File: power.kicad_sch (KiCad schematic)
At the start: 11 parts, among them J2 USB_C_Receptacle_USB2.0_16P, J3 BATTERY, U5 LD1117S33TR_SOT223

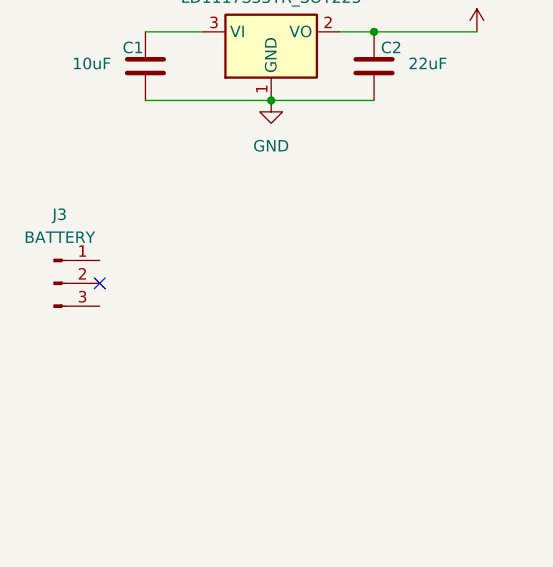
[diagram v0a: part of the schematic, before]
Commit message: battery polarity
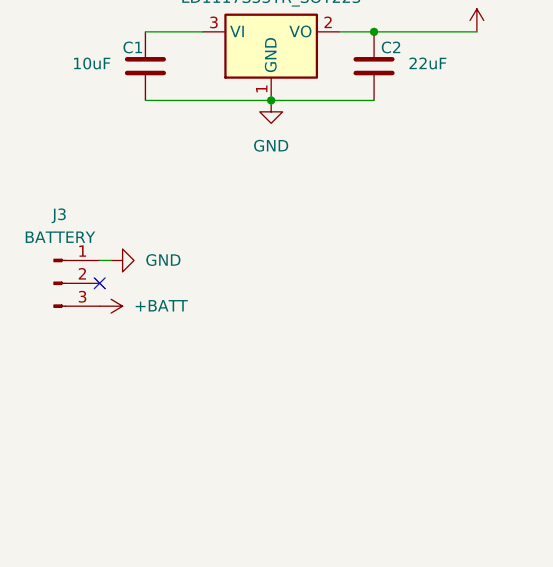
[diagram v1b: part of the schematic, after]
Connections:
- net GND: now also J3.1 (Pin_1)
- net +BATT: now reaches J3.3 (Pin_3)
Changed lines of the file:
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@@
+	(wire
+		(pts
+			(xy 49.53 69.85) (xy 50.8 69.85)
+		)
+		(stroke
+			(width 0)
+			(type default)
+		)
+	)
 	(wire
 		(pts
@@
 	)
 	(symbol
+		(lib_id "power:GND")
+		(at 50.8 69.85 90)
+		(unit 1)
+		(exclude_from_sim no)
+		(in_bom yes)
+		(on_board yes)
+		(dnp no)
+		(fields_autoplaced yes)
+		(property "Reference" "#PWR028"
+			(at 57.15 69.85 0)
+			(effects
+				(font
+					(size 1.27 1.27)
+				)
+				(hide yes)
+			)
+		)
+		(property "Value" "GND"
+			(at 54.61 69.8499 90)
+			(effects
+				(font
+					(size 1.27 1.27)
+				)
+				(justify right)
+			)
+		)
+		(property "Footprint" ""
+			(at 50.8 69.85 0)
+			(effects
+				(font
+					(size 1.27 1.27)
+				)
+				(hide yes)
+			)
+		)
+		(property "Datasheet" ""
+			(at 50.8 69.85 0)
+			(effects
+				(font
+					(size 1.27 1.27)
+				)
+				(hide yes)
+			)
+		)
+		(property "Description" "Power symbol creates a global label with name \"GND\" , ground"
+			(at 50.8 69.85 0)
+			(effects
+				(font
+					(size 1.27 1.27)
+				)
+				(hide yes)
+			)
+		)
+		(pin "1"
+		)
+		(instances
+			(project ""
+				(path "/e9d3405d-3536-4ebc-8db6-e75908125fac/41ee46a8-d813-490e-b535-9d8ea207b7f8"
+					(reference "#PWR028")
+					(unit 1)
+				)
+			)
+		)
+	)
+	(symbol
 		(lib_id "Connector:USB_C_Receptacle_USB2.0_16P")
 		(at 167.64 55.88 0)
@@
 					(unit 1)
 				)
+			)
+		)
+	)
+	(symbol
+		(lib_id "power:+BATT")
+		(at 49.53 74.93 270)
+		(unit 1)
+		(exclude_from_sim no)
+		(in_bom yes)
+		(on_board yes)
+		(dnp no)
+		(fields_autoplaced yes)
+		(property "Reference" "#PWR027"
+			(at 45.72 74.93 0)
+			(effects
+				(font
+					(size 1.27 1.27)
+				)
+				(hide yes)
+			)
+		)
+		(property "Value" "+BATT"
+			(at 53.34 74.9299 90)
+			(effects
+				(font
+					(size 1.27 1.27)
+				)
+				(justify left)
+			)
+		)
+		(property "Footprint" ""
+			(at 49.53 74.93 0)
+			(effects
+				(font
+					(size 1.27 1.27)
+				)
+				(hide yes)
+			)
+		)
+		(property "Datasheet" ""
+			(at 49.53 74.93 0)
+			(effects
+				(font
+					(size 1.27 1.27)
+				)
+				(hide yes)
+			)
+		)
+		(property "Description" "Power symbol creates a global label with name \"+BATT\""
+			(at 49.53 74.93 0)
+			(effects
+				(font
+					(size 1.27 1.27)
+				)
+				(hide yes)
+			)
+		)
+		(pin "1"
+		)
+		(instances
+			(project ""
+				(path "/e9d3405d-3536-4ebc-8db6-e75908125fac/41ee46a8-d813-490e-b535-9d8ea207b7f8"
+					(reference "#PWR027")
+					(unit 1)
+				)

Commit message: power
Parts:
- added D4: BAV70, Package_TO_SOT_SMD:SOT-23, symbol Diode:BAV70
- added Q3: IRLML6402, Package_TO_SOT_SMD:SOT-23, symbol Transistor_FET:IRLML6402
- added R15: 100k, symbol Device:R
- added R16: 1k, symbol Device:R
- added R17: 10k, symbol Device:R
- added SW20: POWER_BUTTON, symbol Switch:SW_Push
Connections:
- net +3.3V: now also R17.1
- net +BATT: now also Q3.2 (S), R15.2
- net GND: now also SW20.1
- net at C1.1, U5.3 (VI): now also Q3.3 (D)
- new net: D4.2 (A), Q3.1 (G), R15.1, R16.2
- new net: D4.3 (K), SW20.2
- new net PWRBTN_DETECT: D4.1 (A), R17.2
- new net PWR_HOLD: R16.1
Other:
- moved on the sheet: C1, C2, J3, U5

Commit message: spi joke
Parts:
- added C8, C9: 1uF, symbol Device:C
- added R23: 1k, symbol Device:R
- added R24: 10k, symbol Device:R
- added TH1: NTC, symbol Device:Thermistor_NTC
- added U4: BQ21040DBV, Package_TO_SOT_SMD:SOT-23-6, symbol Battery_Management:BQ21040DBV
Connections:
- net +3.3V: now also R24.2
- net +BATT: now also C9.1, U4.2 (OUT)
- net GND: now also C8.2, C9.2, R23.2, TH1.2, U4.5 (GND)
- net USB_VBUS: now also C8.1, U4.6 (VIN)
- new net: R23.1, U4.4 (ISET)
- new net: TH1.1, U4.1 (TS)
- new net CHG_PIN: R24.1, U4.3 (~{CHG})

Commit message: buck converter
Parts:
- removed U5: LD1117S33TR_SOT223, Package_TO_SOT_SMD:SOT-223-3_TabPin2, symbol Regulator_Linear:LD1117S33TR_SOT223
- added C13: 22uF 16V X5R, Capacitor_SMD:C_1206_3216Metric, symbol Device:C
- added L1: 2.2uH, Inductor_SMD:L_6.3x6.3_H3, symbol Device:L_Iron
- added R26: 249k, symbol Device:R
- added R27: 54.9k, symbol Device:R
- added TP7: BATTERY, symbol Connector:TestPoint
- added U7: RT8059, Package_TO_SOT_SMD:TSOT-23-5_HandSoldering, symbol RT8059:RT8059
- C1: value 10uF -> 4.7uF; footprint (none) -> Capacitor_SMD:C_0603_1608Metric
- C2: value 22uF -> 0-8.2pF; footprint (none) -> Capacitor_SMD:C_0603_1608Metric_Pad1.08x0.95mm_HandSolder
- R4: footprint (none) -> Capacitor_SMD:C_0603_1608Metric_Pad1.08x0.95mm_HandSolder
- TH1: footprint (none) -> Connector_JST:JST_EH_B2B-EH-A_1x02_P2.50mm_Vertical
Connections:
- net +3.3V: now also C13.1, L1.2, R26.1
- net +BATT: now also TP7.1
- net GND: now also C13.2, R27.2, U7.2 (GND); no longer C2.2
- net at C1.1, Q3.3 (D): now also U7.1 (EN), U7.4 (VIN)
- new net: C2.2, R26.2, R27.1, U7.5 (FB)
- new net: L1.1, U7.3 (LX)
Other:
- moved on the sheet: D1, F1, J2, R4, R5, R6, R7

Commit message: eee:
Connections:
- net +VSW: now reaches C1.1, Q3.3 (D), U7.1 (EN), U7.4 (VIN)
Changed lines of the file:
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@@
+	(wire
+		(pts
+			(xy 152.4 72.39) (xy 152.4 74.93)
+		)
+		(stroke
+			(width 0)
+			(type default)
+		)
+	)
 	(wire
 		(pts
@@
 		(pts
 			(xy 58.42 153.67) (xy 58.42 154.94)
-		)
-		(stroke
-			(width 0)
-			(type default)
-		)
-	)
-	(wire
-		(pts
-			(xy 152.4 74.93) (xy 153.67 74.93)
 		)
 		(stroke
@@
 	(symbol
 		(lib_id "power:+3.3V")
-		(at 153.67 74.93 0)
+		(at 152.4 72.39 0)
 		(unit 1)
 		(exclude_from_sim no)
@@
 		(fields_autoplaced yes)
 		(property "Reference" "#PWR016"
-			(at 153.67 78.74 0)
+			(at 152.4 76.2 0)
 			(effects
 				(font
@@
 		)
 		(property "Value" "+3.3V"
-			(at 153.67 69.85 0)
+			(at 152.4 67.31 0)
 			(effects
 				(font
@@
 		)
 		(property "Footprint" ""
-			(at 153.67 74.93 0)
+			(at 152.4 72.39 0)
 			(effects
 				(font
@@
 		)
 		(property "Datasheet" ""
-			(at 153.67 74.93 0)
+			(at 152.4 72.39 0)
 			(effects
 				(font
@@
 		)
 		(property "Description" "Power symbol creates a global label with name \"+3.3V\""
-			(at 153.67 74.93 0)
+			(at 152.4 72.39 0)
 			(effects
 				(font
@@
 					(unit 1)
 				)
+			)
+		)
+	)
+	(symbol
+		(lib_id "power:+VSW")
+		(at 82.55 74.93 0)
+		(unit 1)
+		(exclude_from_sim no)
+		(in_bom yes)
+		(on_board yes)
+		(dnp no)
+		(fields_autoplaced yes)
+		(property "Reference" "#PWR042"
+			(at 82.55 78.74 0)
+			(effects
+				(font
+					(size 1.27 1.27)
+				)
+				(hide yes)
+			)
+		)
+		(property "Value" "+VSW"
+			(at 82.55 69.85 0)
+			(effects
+				(font
+					(size 1.27 1.27)
+				)
+			)
+		)
+		(property "Footprint" ""
+			(at 82.55 74.93 0)
+			(effects
+				(font
+					(size 1.27 1.27)
+				)
+				(hide yes)
+			)
+		)
+		(property "Datasheet" ""
+			(at 82.55 74.93 0)
+			(effects
+				(font
+					(size 1.27 1.27)
+				)
+				(hide yes)
+			)
+		)
+		(property "Description" "Power symbol creates a global label with name \"+VSW\""
+			(at 82.55 74.93 0)
+			(effects
+				(font
+					(size 1.27 1.27)
+				)
+				(hide yes)
+			)
+		)
+		(pin "1"
+		)
+		(instances
+			(project ""
+				(path "/e9d3405d-3536-4ebc-8db6-e75908125fac/41ee46a8-d813-490e-b535-9d8ea207b7f8"
+					(reference "#PWR042")
+					(unit 1)
+				)

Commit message: mblya
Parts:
- removed J2: USB_C_Receptacle_USB2.0_16P, symbol Connector:USB_C_Receptacle_USB2.0_16P
- removed Q3: IRLML6402, Package_TO_SOT_SMD:SOT-23, symbol Transistor_FET:IRLML6402
- added D4, D5: D_TVS, symbol Device:D_TVS
- added J5: USB_C_Receptacle_USB2.0_16P, symbol Connector:USB_C_Receptacle_USB2.0_16P
- renumbered C8 to C1, C9 to C2, C1 to C3, C2 to C4, C13 to C5, D4 to D1, D1 to D2, R24 to R10, R26 to R11, R27 to R12, R23 to R2, R17 to R3, R6 to R4, R15 to R5, R4 to R6, R5 to R7, R7 to R8, R16 to R9, U7 to U6
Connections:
- net +BATT: now also C3.1, U6.4 (VIN)
- net GND: now also R6.1, R7.1, D4.1 (A1), D5.1 (A1), J5.A1 (GND), J5.A12 (GND), J5.B1 (GND), J5.B12 (GND), J5.S1 (SHIELD); no longer R6.2, R7.2
- net USB_DN: now also D5.2 (A2), J5.A7 (D-), J5.B7 (D-)
- net USB_DP: now also D4.2 (A2), J5.A6 (D+), J5.B6 (D+)
- net at D2.2 (A2), F1.1: now also J5.A4 (VBUS), J5.A9 (VBUS), J5.B4 (VBUS), J5.B9 (VBUS)
- net at D1.2 (A), R5.1, R9.2: now also U6.1 (EN)
- net at R8.1: now also J5.A8 (SBU1)
- net at R4.1: now also J5.B8 (SBU2)
- removed net +VSW: C3.1, U6.1 (EN), U6.4 (VIN)
- new net: J5.A5 (CC1), R6.2
- new net: J5.B5 (CC2), R7.2
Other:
- moved on the sheet: D2, R4, R6, R7, R8

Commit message: SCHEMATIC
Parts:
- added BUCK_BAT, BUCK_POST, BUCK_VBUS, CHRG_VBUS: SolderJumper_2_Open, Jumper:SolderJumper-2_P1.3mm_Open_Pad1.0x1.5mm, symbol Jumper:SolderJumper_2_Open
- R2: value 1k -> 680
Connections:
- net +3.3V: now also BUCK_POST.1 (A); no longer C4.1, L1.2, R11.1
- net +BATT: now also BUCK_BAT.2 (B); no longer C3.1, U6.4 (VIN)
- net USB_VBUS: now also BUCK_VBUS.1 (A), CHRG_VBUS.1 (A); no longer C1.1, U4.6 (VIN)
- new net: BUCK_POST.2 (B), C4.1, L1.2, R11.1
- new net: BUCK_BAT.1 (A), BUCK_VBUS.2 (B), C3.1, U6.4 (VIN)
- new net: C1.1, CHRG_VBUS.2 (B), U4.6 (VIN)
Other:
- note added: "USB"

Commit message: PCB BEGINNNING
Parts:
- C1, C2: footprint (none) -> Capacitor_SMD:C_0603_1608Metric_Pad1.08x0.95mm_HandSolder
- C3: footprint Capacitor_SMD:C_0603_1608Metric -> Capacitor_SMD:C_0603_1608Metric_Pad1.08x0.95mm_HandSolder
- D2, D4, D5: footprint (none) -> Diode_SMD:D_0603_1608Metric_Pad1.05x0.95mm_HandSolder
- F1: footprint (none) -> Fuse:Fuse_1210_3225Metric
- J5: footprint (none) -> UJ20-C-G-MSMT-TR-68:CUI_UJ20-C-G-MSMT-TR-68
- R10, R11, R12, R2, R3, R4, R5, R7, R8, R9: footprint (none) -> Resistor_SMD:R_0603_1608Metric_Pad0.98x0.95mm_HandSolder
- R6: footprint Capacitor_SMD:C_0603_1608Metric_Pad1.08x0.95mm_HandSolder -> Resistor_SMD:R_0603_1608Metric_Pad0.98x0.95mm_HandSolder
- SW20: footprint (none) -> PTS526_SM08_SMTR2_LFS:SW_PTS526_SM08_SMTR2_LFS
- TP7: footprint (none) -> TestPoint:TestPoint_Pad_D1.0mm
- renumbered BUCK_BAT to BUCK_BAT1, BUCK_POST to BUCK_POST1, BUCK_VBUS to BUCK_VBUS1, CHRG_VBUS to CHRG_VBUS1
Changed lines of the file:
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@@
 			)
 		)
-		(property "Footprint" ""
+		(property "Footprint" "Diode_SMD:D_0603_1608Metric_Pad1.05x0.95mm_HandSolder"
 			(at 76.2 173.99 0)
 			(effects
@@
 			)
 		)
-		(property "Footprint" ""
+		(property "Footprint" "Resistor_SMD:R_0603_1608Metric_Pad0.98x0.95mm_HandSolder"
 			(at 32.512 104.14 90)
 			(effects
@@
 			)
 		)
-		(property "Footprint" ""
+		(property "Footprint" "Diode_SMD:D_0603_1608Metric_Pad1.05x0.95mm_HandSolder"
 			(at 71.12 173.99 0)
 			(effects
@@
 			)
 		)
-		(property "Footprint" ""
+		(property "Footprint" "Diode_SMD:D_0603_1608Metric_Pad1.05x0.95mm_HandSolder"
 			(at 83.82 173.99 0)
 			(effects
@@
 			)
 		)
-		(property "Footprint" ""
+		(property "Footprint" "Resistor_SMD:R_0603_1608Metric_Pad0.98x0.95mm_HandSolder"
 			(at 140.462 95.25 90)
 			(effects
@@
 			)
 		)
-		(property "Footprint" "Capacitor_SMD:C_0603_1608Metric"
+		(property "Footprint" "Capacitor_SMD:C_0603_1608Metric_Pad1.08x0.95mm_HandSolder"
 			(at 87.3252 82.55 0)
 			(effects
@@
 			)
 		)
-		(property "Footprint" ""
+		(property "Footprint" "Resistor_SMD:R_0603_1608Metric_Pad0.98x0.95mm_HandSolder"
 			(at 60.452 71.12 90)
 			(effects
@@
 			)
 		)
-		(property "Footprint" ""
+		(property "Footprint" "Resistor_SMD:R_0603_1608Metric_Pad0.98x0.95mm_HandSolder"
 			(at 55.372 43.18 90)
 			(effects
@@
 			)
 		)
-		(property "Footprint" "Capacitor_SMD:C_0603_1608Metric_Pad1.08x0.95mm_HandSolder"
+		(property "Footprint" "Resistor_SMD:R_0603_1608Metric_Pad0.98x0.95mm_HandSolder"
 			(at 66.548 173.99 90)
 			(effects
@@
 			)
 		)
-		(property "Footprint" ""
+		(property "Footprint" "Fuse:Fuse_1210_3225Metric"
 			(at 93.98 138.43 0)
 			(effects
@@
 			)
 		)
-		(property "Footprint" ""
+		(property "Footprint" "PTS526_SM08_SMTR2_LFS:SW_PTS526_SM08_SMTR2_LFS"
 			(at 52.07 52.07 0)
 			(effects
@@
 			)
 		)
-		(property "Footprint" ""
+		(property "Footprint" "Capacitor_SMD:C_0603_1608Metric_Pad1.08x0.95mm_HandSolder"
 			(at 62.23 87.9348 0)
 			(effects
@@
 		(on_board yes)
 		(dnp no)
-		(property "Reference" "BUCK_VBUS"
+		(property "Reference" "BUCK_VBUS1"
 			(at 85.09 72.136 0)
 			(effects
@@
 			(project "okabephone"
 				(path "/e9d3405d-3536-4ebc-8db6-e75908125fac/4fc341b7-aab9-4bf1-942c-802f704f4f3e"
-					(reference "BUCK_VBUS")
+					(reference "BUCK_VBUS1")
 					(unit 1)
 				)
@@
 		(on_board yes)
 		(dnp no)
-		(property "Reference" "BUCK_BAT"
+		(property "Reference" "BUCK_BAT1"
 			(at 62.992 76.454 0)
 			(effects
@@
 			(project "okabephone"
 				(path "/e9d3405d-3536-4ebc-8db6-e75908125fac/4fc341b7-aab9-4bf1-942c-802f704f4f3e"
-					(reference "BUCK_BAT")
+					(reference "BUCK_BAT1")
 					(unit 1)
 				)
@@
 			)
 		)
-		(property "Footprint" ""
+		(property "Footprint" "Resistor_SMD:R_0603_1608Metric_Pad0.98x0.95mm_HandSolder"
 			(at 80.518 107.95 90)
 			(effects
@@
 			)
 		)
-		(property "Footprint" ""
+		(property "Footprint" "Resistor_SMD:R_0603_1608Metric_Pad0.98x0.95mm_HandSolder"
 			(at 54.102 173.99 90)
 			(effects
@@
 			)
 		)
-		(property "Footprint" ""
+		(property "Footprint" "Resistor_SMD:R_0603_1608Metric_Pad0.98x0.95mm_HandSolder"
 			(at 62.738 173.99 90)
 			(effects
@@
 			)
 		)
-		(property "Footprint" ""
+		(property "Footprint" "UJ20-C-G-MSMT-TR-68:CUI_UJ20-C-G-MSMT-TR-68"
 			(at 35.56 154.94 0)
 			(effects
@@
 			)
 		)
-		(property "Footprint" ""
+		(property "Footprint" "Resistor_SMD:R_0603_1608Metric_Pad0.98x0.95mm_HandSolder"
 			(at 140.462 81.28 90)
 			(effects
@@
 		(on_board yes)
 		(dnp no)
-		(property "Reference" "CHRG_VBUS"
+		(property "Reference" "CHRG_VBUS1"
 			(at 25.4 88.646 0)
 			(effects
@@
 			(project "okabephone"
 				(path "/e9d3405d-3536-4ebc-8db6-e75908125fac/4fc341b7-aab9-4bf1-942c-802f704f4f3e"
-					(reference "CHRG_VBUS")
+					(reference "CHRG_VBUS1")
 					(unit 1)
 				)
@@
 		(on_board yes)
 		(dnp no)
-		(property "Reference" "BUCK_POST"
+		(property "Reference" "BUCK_POST1"
 			(at 136.652 76.454 0)
 			(effects
@@
 			(project "okabephone"
 				(path "/e9d3405d-3536-4ebc-8db6-e75908125fac/4fc341b7-aab9-4bf1-942c-802f704f4f3e"
-					(reference "BUCK_POST")
+					(reference "BUCK_POST1")
 					(unit 1)
 				)
@@
 			)
 		)
-		(property "Footprint" ""
+		(property "Footprint" "Capacitor_SMD:C_0603_1608Metric_Pad1.08x0.95mm_HandSolder"
 			(at 26.3652 102.87 0)
 			(effects
@@
 			)
 		)
-		(property "Footprint" ""
+		(property "Footprint" "Resistor_SMD:R_0603_1608Metric_Pad0.98x0.95mm_HandSolder"
 			(at 50.292 173.99 90)
 			(effects
@@
 			)
 		)
-		(property "Footprint" ""
+		(property "Footprint" "Resistor_SMD:R_0603_1608Metric_Pad0.98x0.95mm_HandSolder"
 			(at 71.882 63.5 90)
 			(effects
@@
 			)
 		)
-		(property "Footprint" ""
+		(property "Footprint" "TestPoint:TestPoint_Pad_D1.0mm"
 			(at 41.91 81.28 0)
 			(effects
